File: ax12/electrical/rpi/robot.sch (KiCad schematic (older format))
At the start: 10 parts, among them J1 Raspberry_Pi_2_3, J2 IMU, J3 Power 5V/5A, J6 Power/Data Input, J7 Audio, Q1 BSS138, U2 74LVC1G125, U3 74LVC1G126

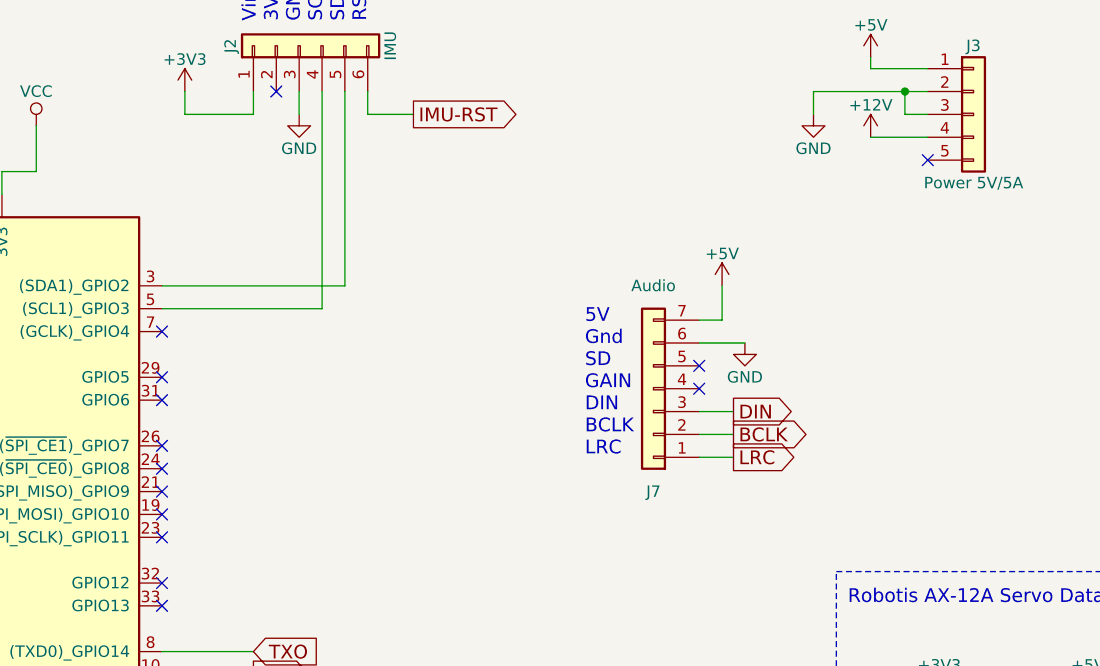
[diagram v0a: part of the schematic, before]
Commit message: updated pi board
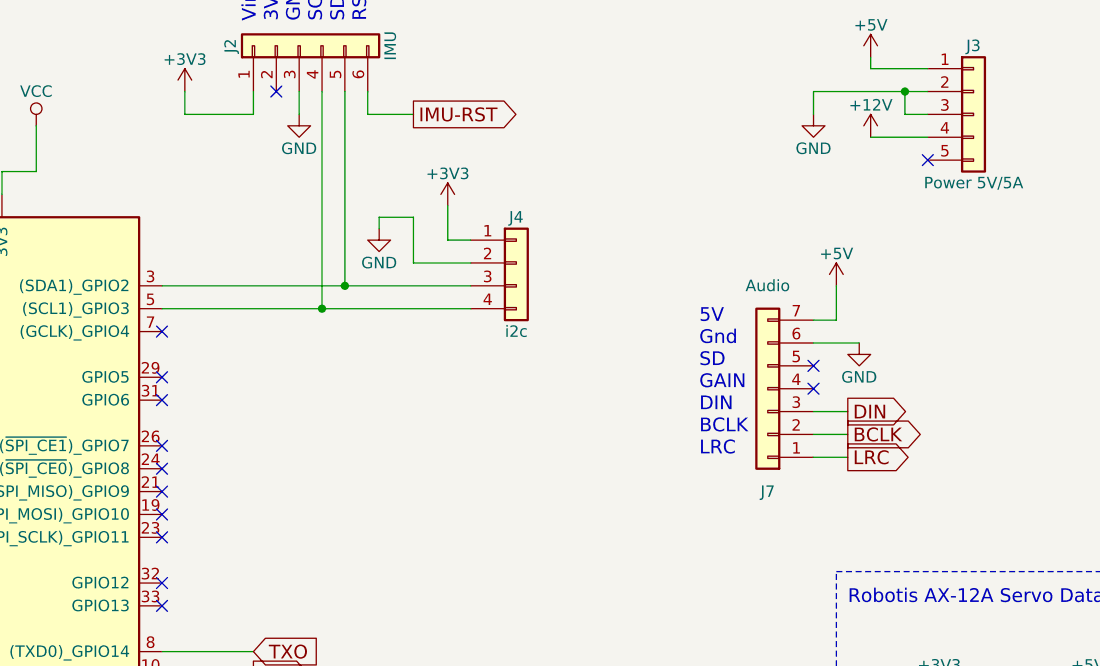
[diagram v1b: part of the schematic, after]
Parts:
- added J4: i2c, Pin_Headers:Pin_Header_Straight_1x04_Pitch2.54mm, symbol Conn_01x04
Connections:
- net +3V3: now also J4.1 (Pin_1)
- net GND: now also J4.2 (Pin_2)
- net at J1.3 ((SDA1)_GPIO2), J2.5 (Pin_5): now also J4.3 (Pin_3)
- net at J1.5 ((SCL1)_GPIO3), J2.4 (Pin_4): now also J4.4 (Pin_4)
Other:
- moved on the sheet: J7
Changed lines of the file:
@@
 L Conn_01x07 J7
 U 1 1 5A93A68D
-P 6550 2500
-F 0 "J7" H 6550 2950 50  0000 C CNN
-F 1 "Audio" H 6550 2050 50  0000 C CNN
-F 2 "Pin_Headers:Pin_Header_Straight_1x07_Pitch2.54mm" H 6550 2500 50  0001 C CNN
-F 3 "" H 6550 2500 50  0001 C CNN
-	1    6550 2500
+P 7050 2500
+F 0 "J7" H 7050 2950 50  0000 C CNN
+F 1 "Audio" H 7050 2050 50  0000 C CNN
+F 2 "Pin_Headers:Pin_Header_Straight_1x07_Pitch2.54mm" H 7050 2500 50  0001 C CNN
+F 3 "" H 7050 2500 50  0001 C CNN
+	1    7050 2500
 	-1   0    0    1
 $EndComp
@@
 Text Notes 1500 1550 0    60   ~ 0
 Pins: Pi (BCM)
-Text Notes 6250 2800 0    60   ~ 0
+Text Notes 6750 2800 0    60   ~ 0
 5V\nGnd\nSD\nGAIN\nDIN\nBCLK\nLRC
 $Comp
 L +5V #PWR05
 U 1 1 5AA19E12
-P 6850 2050
-F 0 "#PWR05" H 6850 1900 50  0001 C CNN
-F 1 "+5V" H 6850 2190 50  0000 C CNN
-F 2 "" H 6850 2050 50  0001 C CNN
-F 3 "" H 6850 2050 50  0001 C CNN
-	1    6850 2050
+P 7350 2050
+F 0 "#PWR05" H 7350 1900 50  0001 C CNN
+F 1 "+5V" H 7350 2190 50  0000 C CNN
+F 2 "" H 7350 2050 50  0001 C CNN
+F 3 "" H 7350 2050 50  0001 C CNN
+	1    7350 2050
 	1    0    0    -1
 $EndComp
@@
 L GND #PWR06
 U 1 1 5AA19E3A
-P 6950 2300
-F 0 "#PWR06" H 6950 2050 50  0001 C CNN
-F 1 "GND" H 6950 2150 50  0000 C CNN
-F 2 "" H 6950 2300 50  0001 C CNN
-F 3 "" H 6950 2300 50  0001 C CNN
-	1    6950 2300
-	1    0    0    -1
-$EndComp
-Text GLabel 6900 2800 2    60   Output ~ 0
+P 7450 2300
+F 0 "#PWR06" H 7450 2050 50  0001 C CNN
+F 1 "GND" H 7450 2150 50  0000 C CNN
+F 2 "" H 7450 2300 50  0001 C CNN
+F 3 "" H 7450 2300 50  0001 C CNN
+	1    7450 2300
+	1    0    0    -1
+$EndComp
+Text GLabel 7400 2800 2    60   Output ~ 0
 LRC
-Text GLabel 6900 2700 2    60   Output ~ 0
+Text GLabel 7400 2700 2    60   Output ~ 0
 BCLK
-Text GLabel 6900 2600 2    60   Output ~ 0
+Text GLabel 7400 2600 2    60   Output ~ 0
 DIN
-NoConn ~ 6750 2500
-NoConn ~ 6750 2400
+NoConn ~ 7250 2500
+NoConn ~ 7250 2400
 Text GLabel 2100 2750 0    60   Output ~ 0
 DIN
@@
 	2600 2750 2100 2750
 Wire Wire Line
-	6950 2300 6750 2300
-Wire Wire Line
-	6750 2200 6850 2200
-Wire Wire Line
-	6850 2200 6850 2050
-Wire Wire Line
-	6750 2600 6900 2600
-Wire Wire Line
-	6750 2700 6900 2700
-Wire Wire Line
-	6750 2800 6900 2800
+	7450 2300 7250 2300
+Wire Wire Line
+	7250 2200 7350 2200
+Wire Wire Line
+	7350 2200 7350 2050
+Wire Wire Line
+	7250 2600 7400 2600
+Wire Wire Line
+	7250 2700 7400 2700
+Wire Wire Line
+	7250 2800 7400 2800
 Wire Wire Line
 	2600 2450 2100 2450
@@
 NoConn ~ 4400 2450
 Wire Wire Line
-	5200 2050 4400 2050
-Wire Wire Line
-	5100 2150 4400 2150
+	4400 2050 5750 2050
+Wire Wire Line
+	4400 2150 5750 2150
 NoConn ~ 4400 2850
 NoConn ~ 4400 2950
 NoConn ~ 4400 3050
 NoConn ~ 4400 3150
+$Comp
+L Conn_01x04 J4
+U 1 1 5B8893A7
+P 5950 1950
+F 0 "J4" H 5950 2150 50  0000 C CNN
+F 1 "i2c" H 5950 1650 50  0000 C CNN
+F 2 "Pin_Headers:Pin_Header_Straight_1x04_Pitch2.54mm" H 5950 1950 50  0001 C CNN
+F 3 "" H 5950 1950 50  0001 C CNN
+	1    5950 1950
+	1    0    0    -1
+$EndComp
+$Comp
+L +3V3 #PWR022
+U 1 1 5B889400
+P 5650 1700
+F 0 "#PWR022" H 5650 1550 50  0001 C CNN
+F 1 "+3V3" H 5650 1840 50  0000 C CNN
+F 2 "" H 5650 1700 50  0001 C CNN
+F 3 "" H 5650 1700 50  0001 C CNN
+	1    5650 1700
+	1    0    0    -1
+$EndComp
+Connection ~ 5100 2150
+Connection ~ 5200 2050
+$Comp
+L GND #PWR023
+U 1 1 5B8896CA
+P 5350 1800
+F 0 "#PWR023" H 5350 1550 50  0001 C CNN
+F 1 "GND" H 5350 1650 50  0000 C CNN
+F 2 "" H 5350 1800 50  0001 C CNN
+F 3 "" H 5350 1800 50  0001 C CNN
+	1    5350 1800
+	1    0    0    -1
+$EndComp
+Wire Wire Line
+	5350 1800 5350 1750
+Wire Wire Line
+	5350 1750 5500 1750
+Wire Wire Line
+	5500 1750 5500 1950
+Wire Wire Line
+	5500 1950 5750 1950
+Wire Wire Line
+	5750 1850 5650 1850
+Wire Wire Line
+	5650 1850 5650 1700
 $EndSCHEMATC

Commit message: up
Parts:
- removed J1: Raspberry_Pi_2_3, Pin_Headers:Pin_Header_Straight_2x20_Pitch2.54mm, symbol Raspberry_Pi_2_3
- removed J2: IMU, Pin_Headers:Pin_Header_Straight_1x06_Pitch2.54mm, symbol Conn_01x06
- removed J3: Power 5V/5A, Pin_Headers:Pin_Header_Straight_1x05_Pitch2.54mm, symbol Conn_01x05
- removed J7: Audio, Pin_Headers:Pin_Header_Straight_1x07_Pitch2.54mm, symbol Conn_01x07
- added J1: i2c, Pin_Headers:Pin_Header_Straight_1x04_Pitch2.54mm, symbol robot-rescue:Conn_01x04
- added J2: Pi Header, Pin_Headers:Pin_Header_Straight_2x05_Pitch2.54mm, symbol Connector_Generic:Conn_02x05_Odd_Even
- J4: symbol Conn_01x04 -> robot-rescue:Conn_01x04
- J6: symbol Conn_01x03 -> robot-rescue:Conn_01x03
- Q1: symbol BSS138 -> robot-rescue:BSS138
- R2, R3: symbol R -> Device:R
- U2: symbol 74LVC1G125 -> Logic_74xgxx:74LVC1G125
- U3: symbol 74LVC1G126 -> Logic_74xgxx:74LVC1G126
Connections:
- net +12V is gone; now on net +5V: J6.2 (Pin_2)
- net VCC is gone; now on net +3V3: U2.5 (VCC), U3.5 (VCC)
- net +3V3: now also J4.4 (Pin_4), J1.4 (Pin_4), J2.1 (Pin_1); no longer J4.1 (Pin_1)
- net +5V: now also J2.2 (Pin_2), J2.4 (Pin_4)
- net DTR: now also J2.7 (Pin_7)
- net GND: now also J4.3 (Pin_3), J1.3 (Pin_3), J2.6 (Pin_6), J2.9 (Pin_9); no longer J4.2 (Pin_2)
- net RXI: now also J2.10 (Pin_10)
- net TXO: now also J2.8 (Pin_8)
- new net SCL: J1.1 (Pin_1), J2.5 (Pin_5), J4.1 (Pin_1)
- new net SDA: J1.2 (Pin_2), J2.3 (Pin_3), J4.2 (Pin_2)
- no-connect marks 23 -> 0
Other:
- note added: "3V3\nGND\nSDA\nSCL"
- note removed: "5V\nGnd\nSD\nGAIN\nDIN\nBCLK\nLRC"
- note removed: "Pins: Pi (BCM)"
- note removed: "Vin\n3Vo\nGND\nSCL\nSDA\nRST"
- moved on the sheet: J4, J6
